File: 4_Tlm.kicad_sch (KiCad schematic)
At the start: 30 parts, among them J502 Conn_Coaxial, J503 Micro_SD_Card, SW501 SW_Push, U501 W25Q128JVE, U502 RP2040

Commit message: Add files via upload
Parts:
- U503: value (none) -> Ra-08H; symbol Ra-08H:Ai-Thinker_Ra-08H -> Polaris_symbols:Ai-Thinker_Ra-08H
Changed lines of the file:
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@@
 	(text "500mA"
 		(exclude_from_sim no)
-		(at 257.81 111.76 0)
+		(at 273.05 95.25 0)
 		(effects
 			(font
@@
 	)
 	(symbol
-		(lib_id "Ra-08H:Ai-Thinker_Ra-08H")
+		(lib_id "Polaris_symbols:Ai-Thinker_Ra-08H")
 		(at 246.38 92.71 0)
 		(mirror y)
@@
 			)
 		)
-		(property "Value" ""
-			(at 246.38 92.71 0)
+		(property "Value" "Ra-08H"
+			(at 254 110.49 0)
 			(show_name no)
 			(do_not_autoplace no)

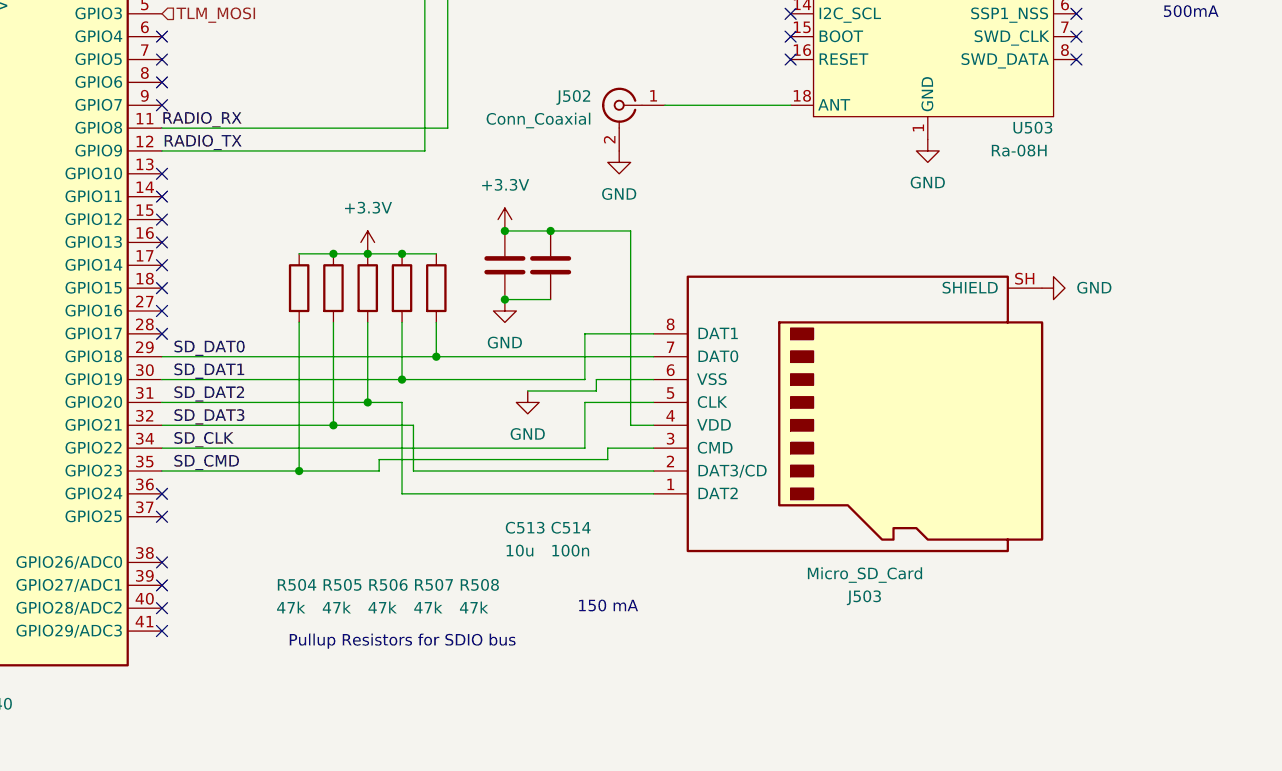
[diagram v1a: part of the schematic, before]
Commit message: Added symbols and footprints Changed schematic to use footprints and symbols from added symbols and footprints
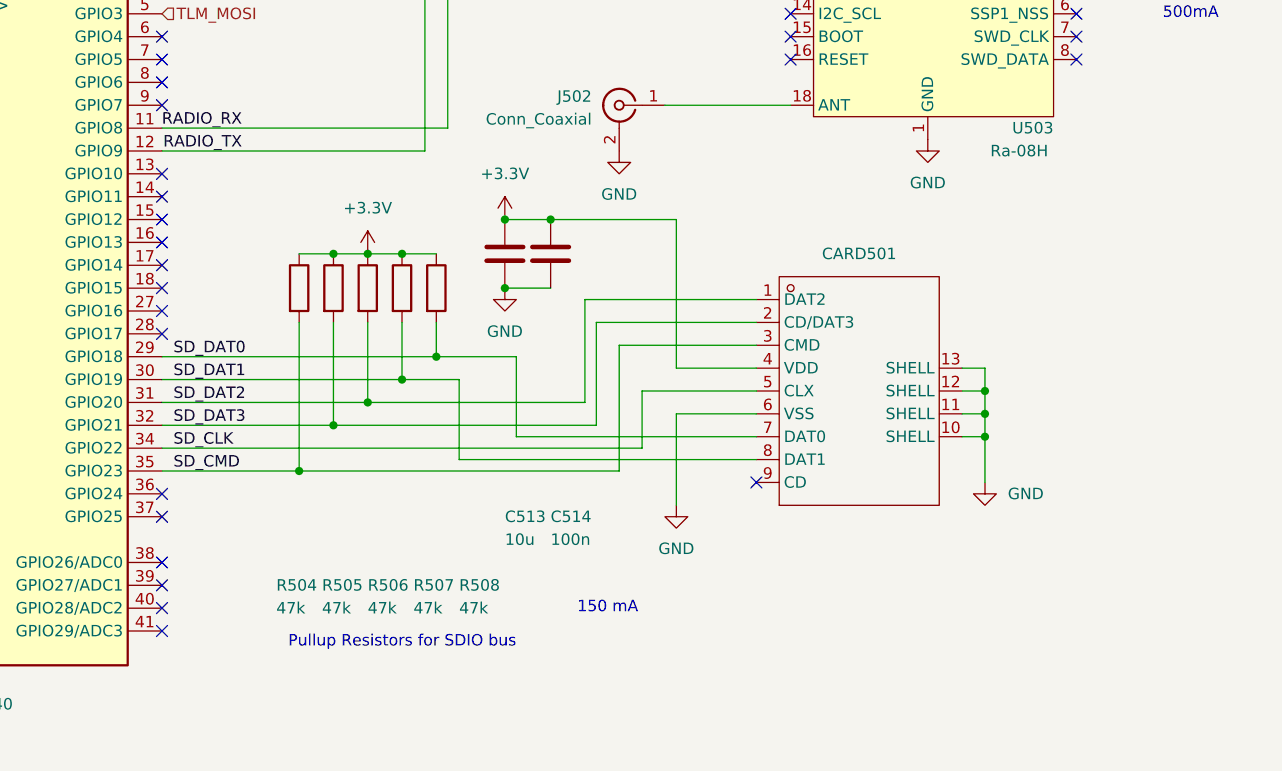
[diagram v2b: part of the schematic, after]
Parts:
- removed J503: Micro_SD_Card, symbol Connector:Micro_SD_Card
- added CARD501: (no value), Polaris:TF-SMD_THD2528-11SD-GF, symbol Polaris_symbols:THD2528-11SD-GF
- J502: footprint (none) -> Connector_Coaxial:SMA_Molex_73251-2200_Horizontal
- SW501: footprint (none) -> Button_Switch_THT:SW_PUSH_6mm
- U503: footprint Ra-08H:RA-08H -> Polaris:RA-08H
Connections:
- net +3.3V: now also CARD501.4 (VDD)
- net GND: now also CARD501.10 (SHELL), CARD501.11 (SHELL), CARD501.12 (SHELL), CARD501.13 (SHELL), CARD501.6 (VSS)
- net SD_CLK: now also CARD501.5 (CLX)
- net SD_CMD: now also CARD501.3 (CMD)
- net SD_DAT0: now also CARD501.7 (DAT0)
- net SD_DAT1: now also CARD501.8 (DAT1)
- net SD_DAT2: now also CARD501.1 (DAT2)
- net SD_DAT3: now also CARD501.2 (CD/DAT3)
- no-connect marks 33 -> 34
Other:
- moved on the sheet: C513, C514

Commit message: Added status LEDs and buzzer for indication
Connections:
- net TLM_STAT1: now reaches U502.13 (GPIO10)
- net TLM_STAT2: now reaches U502.14 (GPIO11)
- net TLM_STAT3: now reaches U502.15 (GPIO12)
- no-connect marks 34 -> 31
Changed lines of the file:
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@@
-	)
-	(no_connect
-		(at 158.75 113.03)
 	)
 	(no_connect
@@
 	)
 	(no_connect
-		(at 158.75 115.57)
-	)
-	(no_connect
 		(at 260.35 87.63)
 	)
@@
 	)
 	(no_connect
+		(at 158.75 120.65)
+	)
+	(no_connect
 		(at 158.75 97.79)
 	)
@@
 	)
 	(no_connect
-		(at 158.75 118.11)
-	)
-	(no_connect
 		(at 158.75 100.33)
 	)
@@
 	)
 	(no_connect
-		(at 158.75 120.65)
-	)
-	(no_connect
 		(at 107.95 151.13)
 	)
@@
 	(wire
 		(pts
+			(xy 158.75 115.57) (xy 172.72 115.57)
+		)
+		(stroke
+			(width 0)
+			(type default)
+		)
+	)
+	(wire
+		(pts
 			(xy 205.74 127) (xy 224.79 127)
 		)
@@
 	(wire
 		(pts
+			(xy 158.75 113.03) (xy 172.72 113.03)
+		)
+		(stroke
+			(width 0)
+			(type default)
+		)
+	)
+	(wire
+		(pts
 			(xy 158.75 135.89) (xy 185.42 135.89)
 		)
@@
 		(pts
 			(xy 243.84 69.85) (xy 246.38 69.85)
+		)
+		(stroke
+			(width 0)
+			(type default)
+		)
+	)
+	(wire
+		(pts
+			(xy 158.75 118.11) (xy 172.72 118.11)
 		)
 		(stroke
@@
 		)
 	)
+	(label "TLM_STAT2"
+		(at 172.72 115.57 180)
+		(effects
+			(font
+				(size 1.27 1.27)
+			)
+			(justify right bottom)
+		)
+	)
 	(label "SD_DAT1"
 		(at 160.02 135.89 0)
@@
 		)
 	)
+	(label "TLM_STAT3"
+		(at 172.72 118.11 180)
+		(effects
+			(font
+				(size 1.27 1.27)
+			)
+			(justify right bottom)
+		)
+	)
 	(label "RADIO_TX"
 		(at 167.64 110.49 180)
@@
 		)
 	)
+	(label "TLM_STAT1"
+		(at 172.72 113.03 180)
+		(effects
+			(font
+				(size 1.27 1.27)
+			)
+			(justify right bottom)
+		)
+	)

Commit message: Added status LEDs for TLM (forgot to add previously)
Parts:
- added D502, D503, D504: LED, symbol Device:LED
- added R509, R510, R511: R, Resistor_SMD:R_0603_1608Metric, symbol Device:R
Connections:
- net GND: now also D502.1 (K), D503.1 (K), D504.1 (K)
- net TLM_STAT1: now also R509.1
- net TLM_STAT2: now also R510.1
- net TLM_STAT3: now also R511.1
- new net: D504.2 (A), R511.2
- new net: D503.2 (A), R510.2
- new net: D502.2 (A), R509.2
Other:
- note added: "Status LEDs for TLM"

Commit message: Redid ESD protection because the previous chip couldn't handle 9V from USB-PD Finished status indication sections
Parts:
- D501, D502, D503, D504: footprint (none) -> LED_SMD:LED_0603_1608Metric
- R509, R510, R511: value R -> 180R
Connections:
- net at U502.36 (GPIO24): now also CARD501.9 (CD)
- no-connect marks 31 -> 29
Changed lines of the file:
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@@
 	)
 	(no_connect
-		(at 158.75 148.59)
-	)
-	(no_connect
 		(at 158.75 120.65)
 	)
@@
 	)
 	(no_connect
-		(at 224.79 147.32)
-	)
-	(no_connect
 		(at 260.35 92.71)
 	)
@@
 	(wire
 		(pts
+			(xy 199.39 148.59) (xy 158.75 148.59)
+		)
+		(stroke
+			(width 0)
+			(type default)
+		)
+	)
+	(wire
+		(pts
 			(xy 246.38 77.47) (xy 259.08 77.47)
 		)
@@
 	(wire
 		(pts
+			(xy 224.79 147.32) (xy 199.39 147.32)
+		)
+		(stroke
+			(width 0)
+			(type default)
+		)
+	)
+	(wire
+		(pts
 			(xy 215.9 118.11) (xy 201.93 118.11)
 		)
@@
 	(wire
 		(pts
+			(xy 199.39 147.32) (xy 199.39 148.59)
+		)
+		(stroke
+			(width 0)
+			(type default)
+		)
+	)
+	(wire
+		(pts
 			(xy 171.45 60.96) (xy 179.07 60.96)
 		)
@@
 			)
 		)
-		(property "Value" "R"
+		(property "Value" "180R"
 			(at 45.72 177.8 90)
 			(show_name no)
@@
 			)
 		)
-		(property "Value" "R"
+		(property "Value" "180R"
 			(at 45.72 167.64 90)
 			(show_name no)
@@
 			)
 		)
-		(property "Footprint" ""
+		(property "Footprint" "LED_SMD:LED_0603_1608Metric"
 			(at 53.34 170.18 0)
 			(hide yes)
@@
 			)
 		)
-		(property "Footprint" ""
+		(property "Footprint" "LED_SMD:LED_0603_1608Metric"
 			(at 53.34 160.02 0)
 			(hide yes)
@@
 			)
 		)
-		(property "Value" "R"
+		(property "Value" "180R"
 			(at 45.72 157.48 90)
 			(show_name no)
@@
 			)
 		)
-		(property "Footprint" ""
+		(property "Footprint" "LED_SMD:LED_0603_1608Metric"
 			(at 259.08 73.66 0)
 			(hide yes)
@@
 			)
 		)
-		(property "Footprint" ""
+		(property "Footprint" "LED_SMD:LED_0603_1608Metric"
 			(at 53.34 180.34 0)
 			(hide yes)

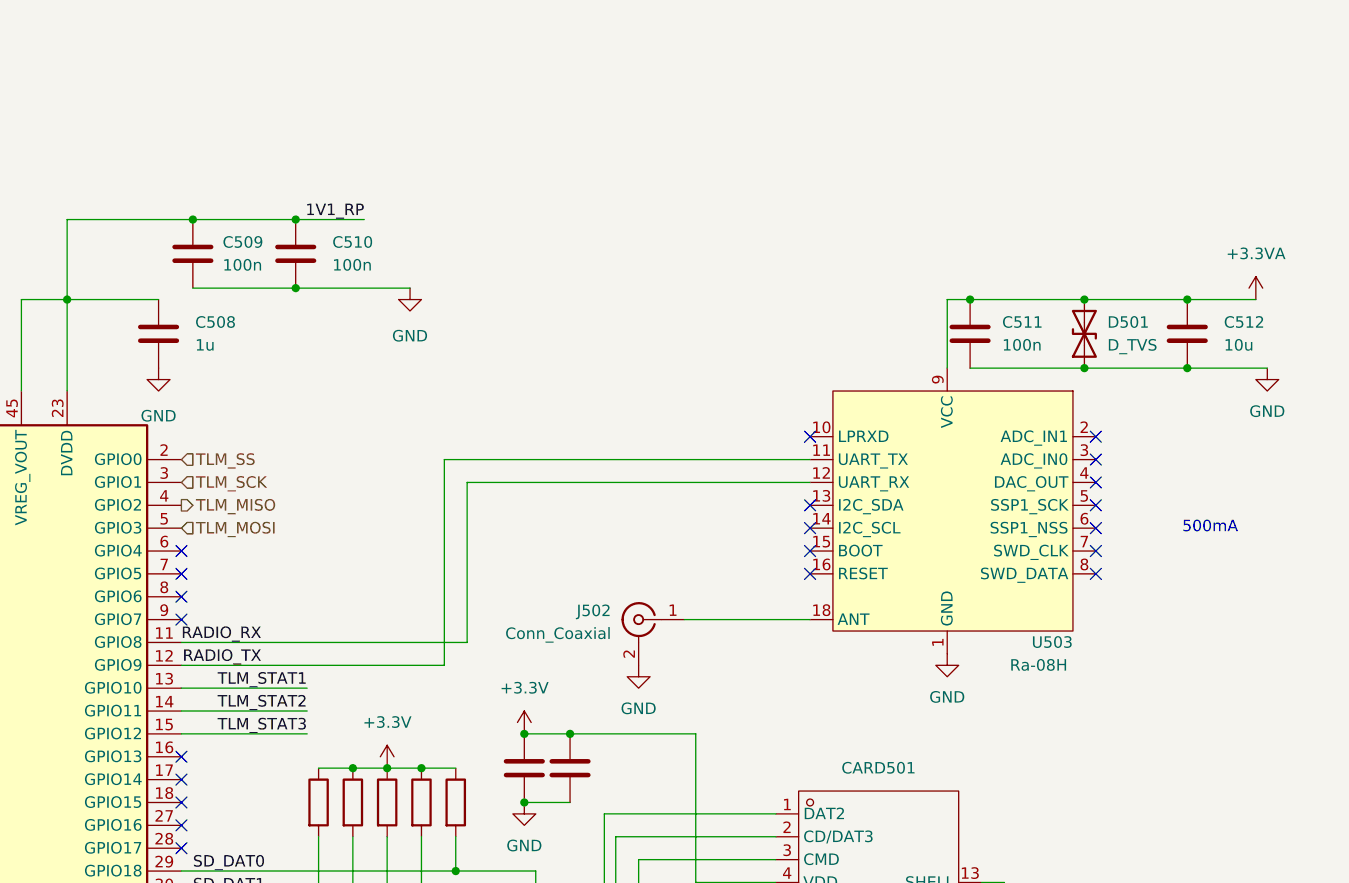
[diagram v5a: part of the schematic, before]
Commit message: Redid LoRa radio section Changed regulator output inductor to 10 uH based on availability
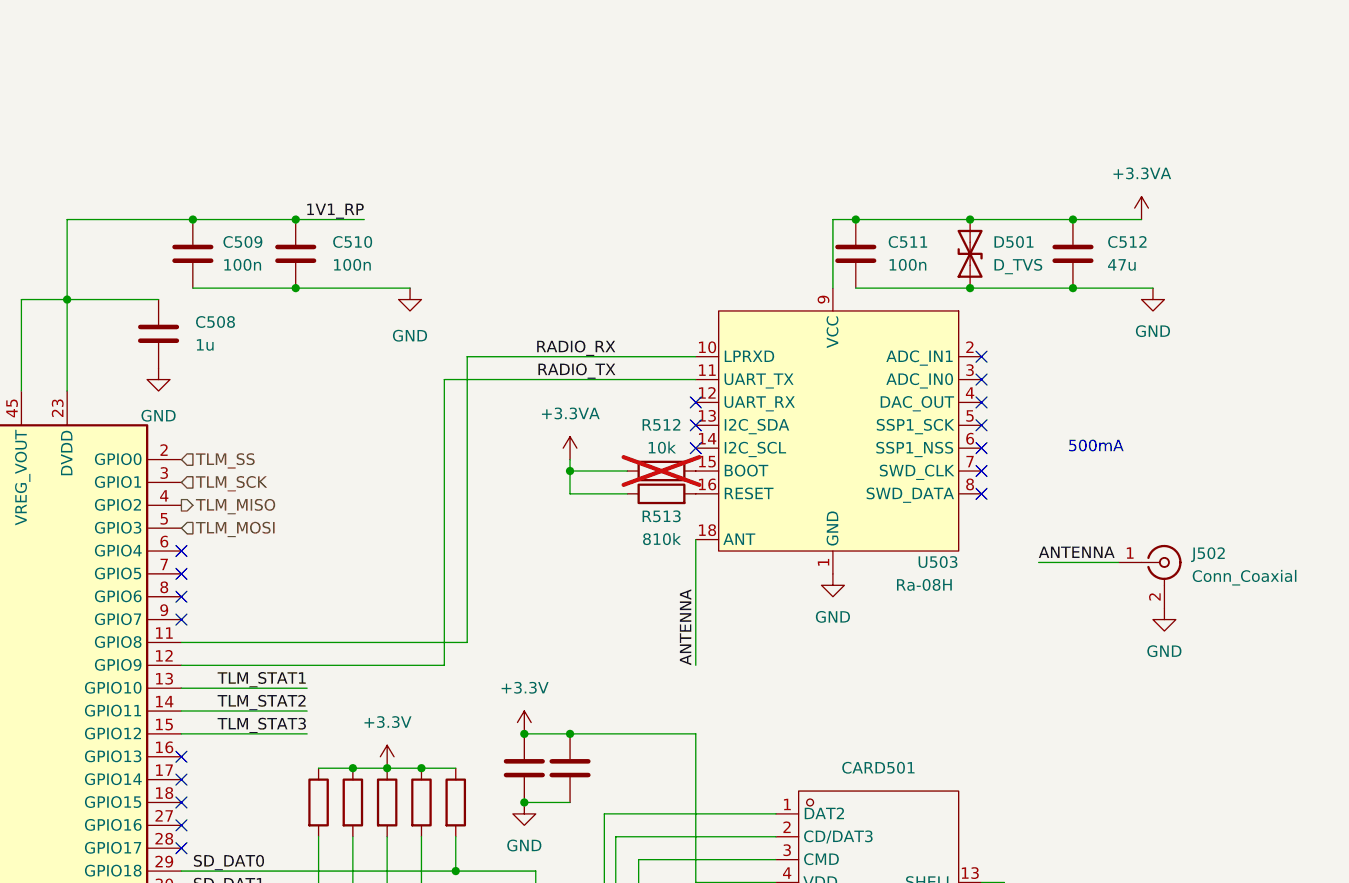
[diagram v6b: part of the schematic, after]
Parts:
- added R512: 10k, symbol Device:R
- added R513: 810k, symbol Device:R
- C512: value 10u -> 47u
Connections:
- net +3.3VA: now also R512.1, R513.1
- net RADIO_RX: now also U503.10 (LPRXD); no longer U503.12 (UART_RX)
- net at U503.15 (BOOT): now also R512.2
- net at U503.16 (RESET): now also R513.2
- net ANTENNA: now reaches J502.1 (In), U503.18 (ANT)
- no-connect marks 29 -> 27
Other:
- moved on the sheet: C511, C512, D501, J502, U503
